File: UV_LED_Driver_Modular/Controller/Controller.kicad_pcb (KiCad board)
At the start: 2 copper layers, 68.6 x 39.4 mm, 19 parts, among them J1 Barrel_Jack, J2 Conn_01x05, J3 Conn_02x06_Odd_Even, Q1 Q_NPN_ECB, Q2 Q_NPN_ECB, SW1 SW_SPST, U1 STM32L011D4Px, U2 LP3992-33B5F

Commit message: updated
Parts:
- removed REF** (x4): MountingHole_3.2mm_M3, MountingHole:MountingHole_3.2mm_M3
- added J4: Conn_01x03, Connector_Molex:Molex_KK-254_AE-6410-03A_1x03_P2.54mm_Vertical, B.Cu at (82.4, 55.4)
- added JP1: Jumper_NC_Small, Jumper:SolderJumper-2_P1.3mm_Bridged_Pad1.0x1.5mm, F.Cu at (96.6, 78.8)
- added Q3: Q_NPN_BCE, Package_TO_SOT_SMD:SOT-223-3_TabPin2, F.Cu at (79.9, 62.9)
- added R5: 1K, Resistor_SMD:R_1206_3216Metric_Pad1.42x1.75mm_HandSolder, F.Cu at (71.5, 61.3)
- added R6: 2K2, Resistor_SMD:R_1206_3216Metric_Pad1.42x1.75mm_HandSolder, F.Cu at (74.0, 61.3)
- Q1, Q2: value Q_NPN_ECB -> Q_NPN_BCE; footprint Package_TO_SOT_THT:TO-220-3_Vertical -> Package_TO_SOT_SMD:SOT-223-3_TabPin2; moved to F.Cu
- moved J1 29.0 mm to (113.8, 53.3), turned to 270 degrees
- moved R2 17.4 mm to (71.5, 70.5), turned to 270 degrees
- moved Q1 16.3 mm to (79.9, 81.3), turned to 180 degrees
- moved R1 16.3 mm to (71.4, 79.8), turned to 270 degrees
- moved R3 16.1 mm to (73.9, 79.8), turned to 270 degrees
- moved C2 14.8 mm to (102.7, 55.0), turned to 90 degrees
- moved R4 13.8 mm to (74.0, 70.5), turned to 270 degrees
- moved C1 8.87 mm to (94.5, 55.0)
- moved U2 8.87 mm to (98.7, 55.5)
- moved Q2 5.11 mm to (79.9, 72.0), turned to 180 degrees
- moved J2 3.91 mm to (95.9, 62.0)
- moved U1 3.17 mm to (102.2, 73.7)
- moved RV1 1.90 mm to (113.7, 64.5)
- moved SW1 1.90 mm to (113.7, 75.9)
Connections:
- net /LED_PWM renamed /LED_PWM_OUT
- net /UV_PWM renamed /UV_PWM_OUT
- Q1 pad 1: /LED_Controller_Module/UV_LED_PWM -> Net-(Q1-Pad1)
- Q1 pad 3: Net-(Q1-Pad3) -> /LED_Controller_Module/UV_LED_PWM
- Q2 pad 1: /LED_Controller_Module/LED_PWM -> Net-(Q2-Pad1)
- Q2 pad 3: Net-(Q2-Pad3) -> /LED_Controller_Module/LED_PWM
- R1 pad 2: Net-(Q1-Pad3) -> Net-(Q1-Pad1)
- R2 pad 2: Net-(Q2-Pad3) -> Net-(Q2-Pad1)
- U1 pad 1: GNDS -> Net-(JP1-Pad2)
- U1 pad 12: Net-(U1-Pad12) -> /LED_Controller_Module/STATUS_PWM
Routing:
- net +5V: track 83.4 -> 190.6 mm, vias 2 -> 0
- net /LED_Controller_Module/UV_LED_PWM: track 77.9 -> 25.0 mm
- net /STATUS_PWM_OUT: track 0.00 -> 46.3 mm, vias 0 -> 2
- net +3V3: track 88.7 -> 116.1 mm
- net /LED_Controller_Module/STATUS_PWM: track 0.00 -> 26.8 mm
- net /UV_PWM_OUT: track 46.0 -> 24.1 mm
- net /LED_Controller_Module/LED_PWM: track 46.9 -> 25.1 mm
- net /LED_PWM_OUT: track 43.6 -> 28.7 mm, vias 0 -> 2
- net Net-(Q1-Pad1): track 0.00 -> 13.5 mm
- net Net-(Q2-Pad1): track 0.00 -> 13.3 mm
- net Net-(Q3-Pad1): track 0.00 -> 13.3 mm
- net Net-(JP1-Pad2): track 0.00 -> 4.78 mm
- net Net-(Q2-Pad3): track 3.42 -> 0.00 mm
- net Net-(Q1-Pad3): track 3.42 -> 0.00 mm
- net GNDS: track 62.1 -> 65.5 mm, vias 7 -> 8
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
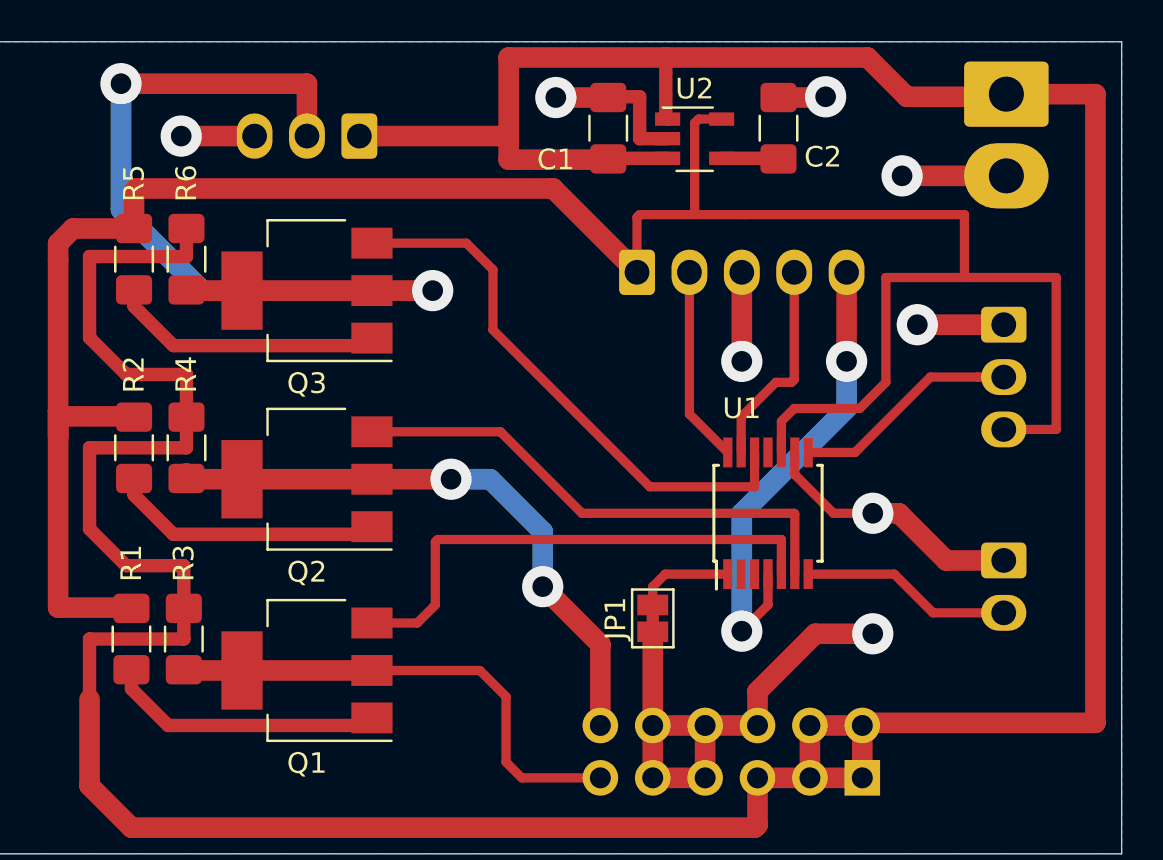
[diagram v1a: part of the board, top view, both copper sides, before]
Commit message: changed controller module LDO from SOT23 to SOT223
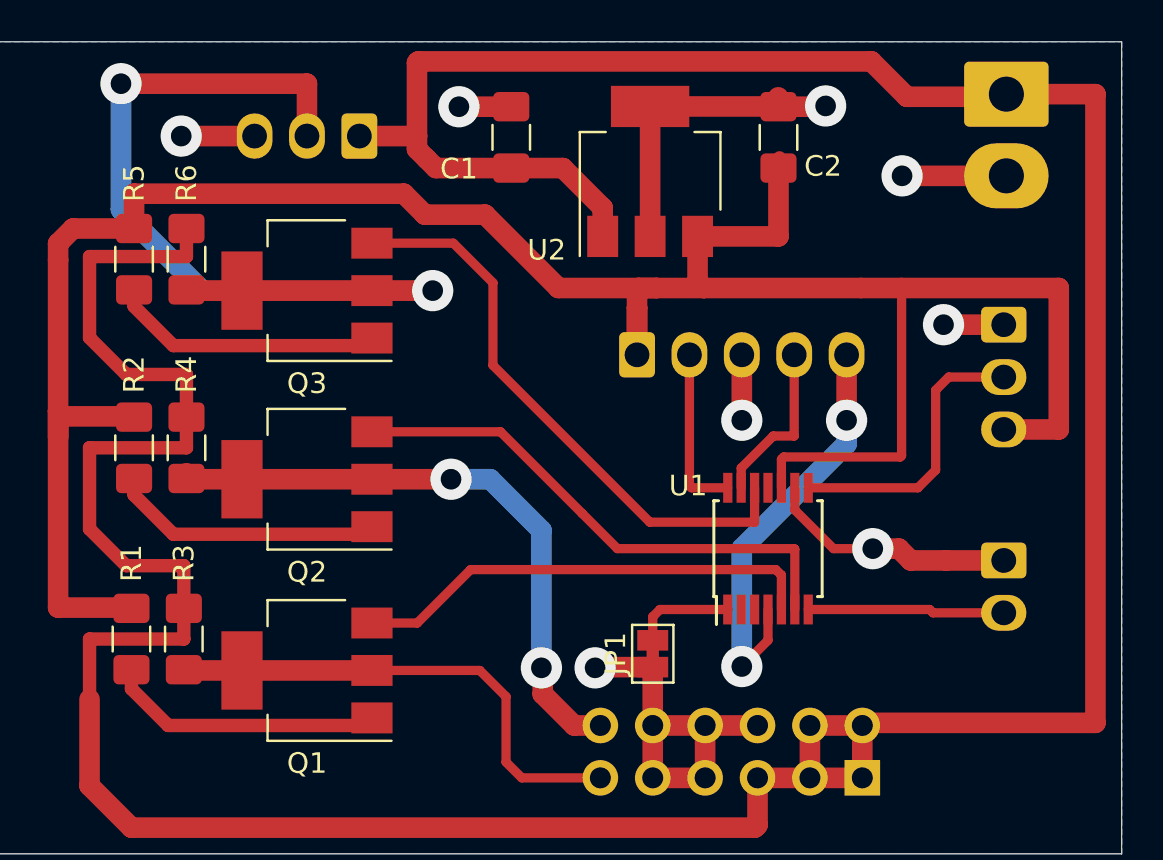
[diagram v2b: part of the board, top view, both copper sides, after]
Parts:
- U2: value LP3992-33B5F -> MCP1703A-3302_SOT223; footprint Package_TO_SOT_SMD:TSOT-23-5 -> Package_TO_SOT_SMD:SOT-223-3_TabPin2
- moved C1 4.72 mm to (89.8, 55.4)
- moved J2 4.00 mm to (95.9, 66.0)
- moved U2 2.68 mm to (96.5, 57.1), turned to 90 degrees
- moved JP1 1.71 mm to (96.6, 80.5)
- moved U1 1.71 mm to (102.2, 75.4)
- moved C2 0.44 mm to (102.7, 55.4)
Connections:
- C2 pad 1: Net-(C2-Pad1) -> +3V3
- U2 pad 3: +5V -> +3V3
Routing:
- net +3V3: track 116.1 -> 119.6 mm
- net /LED_Controller_Module/LED_ADC: track 11.0 -> 14.0 mm
- net Net-(C2-Pad1): track 2.84 -> 0.00 mm
- net GNDS: track 65.5 -> 63.0 mm
- net /LED_Controller_Module/UV_LED_PWM: track 25.0 -> 22.7 mm
- net /LED_Controller_Module/NRST: track 22.8 -> 20.9 mm
- net /LED_Controller_Module/SWDIO: track 10.2 -> 8.49 mm
- net /LED_Controller_Module/STATUS_PWM: track 26.8 -> 28.2 mm
- net /LED_Controller_Module/SWCLK: track 9.50 -> 8.63 mm
- net /LED_PWM_OUT: track 28.7 -> 29.5 mm
- net /LED_Controller_Module/LID_SW: track 10.3 -> 9.55 mm
- net /LED_Controller_Module/LED_PWM: track 25.1 -> 25.8 mm

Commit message: docs update
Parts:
- removed J4: Conn_01x03, Connector_Molex:Molex_KK-254_AE-6410-03A_1x03_P2.54mm_Vertical
- removed Q1, Q2, Q3: Q_NPN_BCE, Package_TO_SOT_SMD:SOT-223-3_TabPin2
- removed R4, R6: 2K2, Resistor_SMD:R_1206_3216Metric_Pad1.42x1.75mm_HandSolder
- removed R5: 1K, Resistor_SMD:R_1206_3216Metric_Pad1.42x1.75mm_HandSolder
- removed RV1: B10K, Connector_Molex:Molex_KK-254_AE-6410-03A_1x03_P2.54mm_Vertical
- added D1: LED_RGBA, Connector_PinHeader_2.54mm:PinHeader_1x04_P2.54mm_Vertical, B.Cu at (61.3, 105.0)
- added REF**: MountingHole_3.2mm_M3, MountingHole:MountingHole_3.2mm_M3, F.Cu at (48.6, 127.4)
- added REF**: MountingHole_3.2mm_M3, MountingHole:MountingHole_3.2mm_M3, F.Cu at (96.3, 105.3)
- added REF**: MountingHole_3.2mm_M3, MountingHole:MountingHole_3.2mm_M3, F.Cu at (48.8, 105.2)
- added REF**: MountingHole_3.2mm_M3, MountingHole:MountingHole_3.2mm_M3, F.Cu at (96.4, 127.4)
- added SW2: Rotary_Encoder, Connector_PinHeader_2.54mm:PinHeader_1x03_P2.54mm_Vertical, B.Cu at (83.0, 117.2)
- J2: footprint Connector_Molex:Molex_KK-254_AE-6410-05A_1x05_P2.54mm_Vertical -> Connector_PinHeader_2.54mm:PinHeader_1x05_P2.54mm_Vertical
- J3: value Conn_02x06_Odd_Even -> Conn_02x08_Odd_Even; footprint Connector_IDC:IDC-Header_2x06_P2.54mm_Vertical -> Connector_PinHeader_2.54mm:PinHeader_2x08_P2.54mm_Vertical
- R1: value 1K -> 2K2
- R2: value 1K -> 10K
- R3: value 2K2 -> 10K
- SW1: footprint Connector_Molex:Molex_KK-254_AE-6410-02A_1x02_P2.54mm_Vertical -> Connector_PinHeader_2.54mm:PinHeader_1x02_P2.54mm_Vertical
- U1: value STM32L011D4Px -> STM32F051K8Tx; footprint Package_SO:TSSOP-14_4.4x5mm_P0.65mm -> Package_QFP:LQFP-32_7x7mm_P0.8mm
- U2: value MCP1703A-3302_SOT223 -> L78L33_SOT89; footprint Package_TO_SOT_SMD:SOT-223-3_TabPin2 -> Package_TO_SOT_SMD:SOT-89-3
- moved SW1 73.7 mm to (54.9, 120.4), turned to 0 degrees
- moved J1 63.5 mm to (95.9, 114.3)
- moved J2 62.8 mm to (89.3, 128.4), turned to 90 degrees
- moved C2 55.5 mm to (89.3, 109.3)
- moved C1 54.8 mm to (79.6, 109.3), turned to 270 degrees
- moved U2 53.6 mm to (84.8, 109.3), turned to 180 degrees
- moved J3 53.5 mm to (72.8, 127.8)
- moved U1 52.2 mm to (65.7, 112.6), turned to 270 degrees
- moved R2 49.5 mm to (87.8, 117.2), turned to 180 degrees
- moved R3 44.7 mm to (87.8, 122.2), turned to 180 degrees
- moved JP1 38.6 mm to (72.5, 110.6), turned to 270 degrees
- moved R1 25.4 mm to (74.3, 105.0), turned to 180 degrees
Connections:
- C1 pad 1: +5V -> VPP
- J1 pad 1: +5V -> VPP
- J3 pad 1: +5V -> /LED_PWM_OUT2
- J3 pad 10: GNDS -> VPP
- J3 pad 11: /UV_PWM_OUT -> VPP
- J3 pad 12: /LED_PWM_OUT -> GNDS
- J3 pad 2: +5V -> /LED_PWM_OUT3
- J3 pad 3: +5V -> /LED_PWM_OUT1
- J3 pad 4: +5V -> /LED_PWM_OUT4
- J3 pad 5: +5V -> Net-(J3-Pad5)
- J3 pad 6: GNDS -> /LED_PWM_OUT5
- J3 pad 7: GNDS -> VPP
- J3 pad 8: GNDS -> VPP
- J3 pad 9: GNDS -> VPP
- R1 pad 1: +3V3 -> VPP
- R2 pad 2: Net-(Q2-Pad1) -> /LED_Controller_Module/ENC_A
- R3 pad 1: +5V -> +3V3
- R3 pad 2: /UV_PWM_OUT -> /LED_Controller_Module/ENC_B
- SW1 pad 2: /LED_Controller_Module/LID_SW -> /LED_Controller_Module/ENABLE_LED
- U1 pad 1: Net-(JP1-Pad2) -> +3V3
- U1 pad 10: +3V3 -> Net-(U1-Pad10)
- U1 pad 12: /LED_Controller_Module/STATUS_PWM -> Net-(U1-Pad12)
- U1 pad 13: /LED_Controller_Module/SWDIO -> Net-(U1-Pad13)
- U1 pad 14: /LED_Controller_Module/SWCLK -> /LED_Controller_Module/ENABLE_LED
- U1 pad 5: /LED_Controller_Module/UV_LED_PWM -> +3V3
- U1 pad 6: /LED_Controller_Module/LED_PWM -> /LED_Controller_Module/STATUS_BLUE
- U1 pad 7: /LED_Controller_Module/LID_SW -> /LED_Controller_Module/STATUS_GREEN
- U1 pad 8: /LED_Controller_Module/LED_ADC -> /LED_Controller_Module/STATUS_RED
- U1 pad 9: GNDS -> Net-(U1-Pad9)
- U2 pad 1: +5V -> +3V3
- U2 pad 3: +3V3 -> VPP
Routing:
- net +5V: track 190.5 -> 0.00 mm
- net VPP: track 0.00 -> 113.6 mm
- net +3V3: track 119.6 -> 62.7 mm
- net /STATUS_PWM_OUT: track 46.3 -> 0.00 mm, vias 2 -> 0
- net /LED_PWM_OUT: track 29.5 -> 0.00 mm, vias 2 -> 0
- net /LED_PWM_OUT1: track 0.00 -> 29.2 mm
- net /LED_Controller_Module/STATUS_PWM: track 28.2 -> 0.00 mm
- net /LED_Controller_Module/LED_PWM: track 25.8 -> 0.00 mm
- net /UV_PWM_OUT: track 24.1 -> 0.00 mm
- net /LED_Controller_Module/UV_LED_PWM: track 22.7 -> 0.00 mm
- net /LED_PWM_OUT2: track 0.00 -> 21.7 mm
- net /LED_Controller_Module/ENC_B: track 0.00 -> 19.4 mm
- net /LED_PWM_OUT5: track 0.00 -> 19.3 mm
- net /LED_Controller_Module/ENC_A: track 0.00 -> 17.7 mm
- net /LED_Controller_Module/SWCLK: track 8.63 -> 25.4 mm
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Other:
- board size 68.6 x 39.4 mm -> 55 x 29.5 mm
